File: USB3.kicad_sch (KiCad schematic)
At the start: 20 parts, among them J1 10152803-00011LF, U1 NCP360SNT1G, U2 TUSB321RWBR, U7 TUSB542RWQR

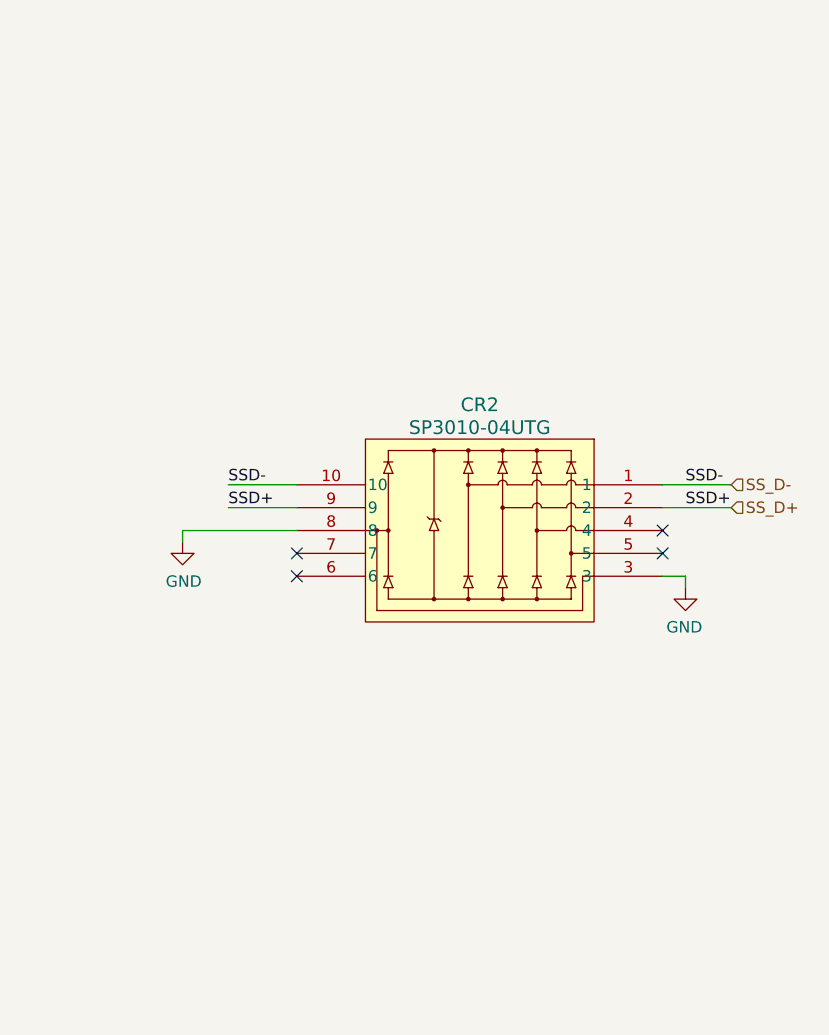
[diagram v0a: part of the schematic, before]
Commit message: start reworking the usb3c to add ESD and better impedance matching
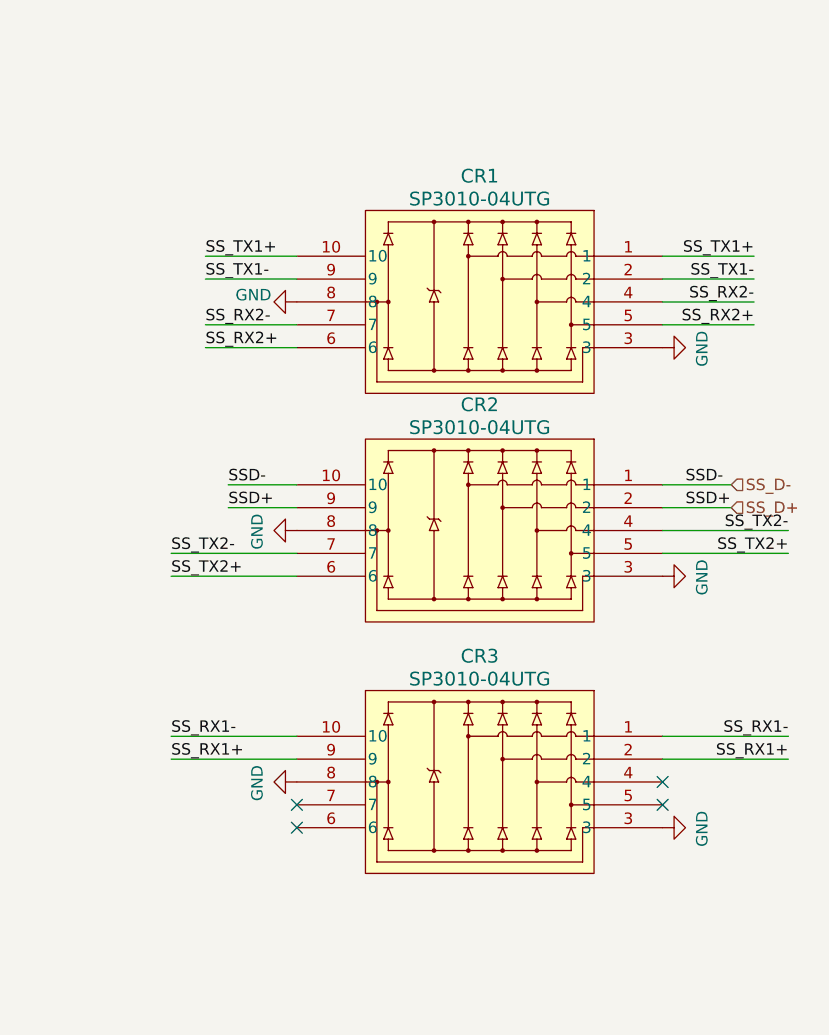
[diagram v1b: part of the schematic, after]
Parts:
- added CR1, CR3: SP3010-04UTG, SP3010:UDFEN-10_MO229_LTF, symbol SP3010-04UTG:SP3010-04UTG
- C69, C70, C71, C72, C73, C74, C8, C9: footprint Capacitor_SMD:C_0402_1005Metric -> Capacitor_SMD:C_0201_0603Metric
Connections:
- net GND: now also CR1.3, CR1.8, CR3.3, CR3.8
- net SS_RX1+: now also CR3.2, CR3.9
- net SS_RX1-: now also CR3.1, CR3.10
- net SS_RX2+: now also CR1.5, CR1.6
- net SS_RX2-: now also CR1.4, CR1.7
- net SS_TX1+: now also CR1.1, CR1.10
- net SS_TX1-: now also CR1.2, CR1.9
- net SS_TX2+: now also CR2.5, CR2.6
- net SS_TX2-: now also CR2.4, CR2.7

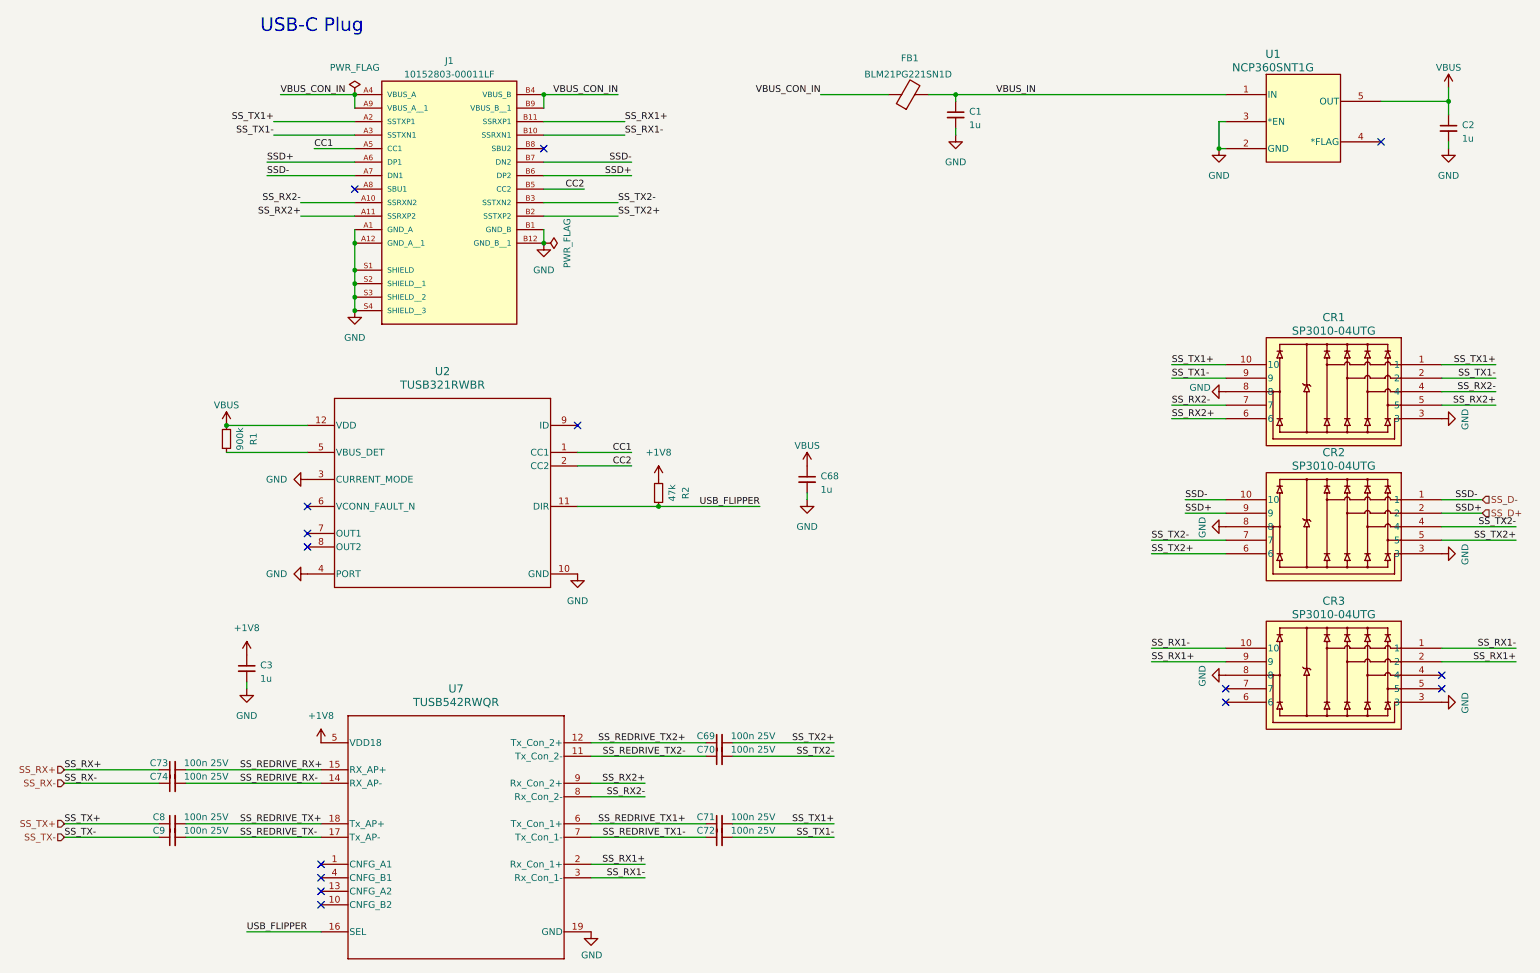
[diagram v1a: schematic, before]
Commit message: start implementing SML feedback
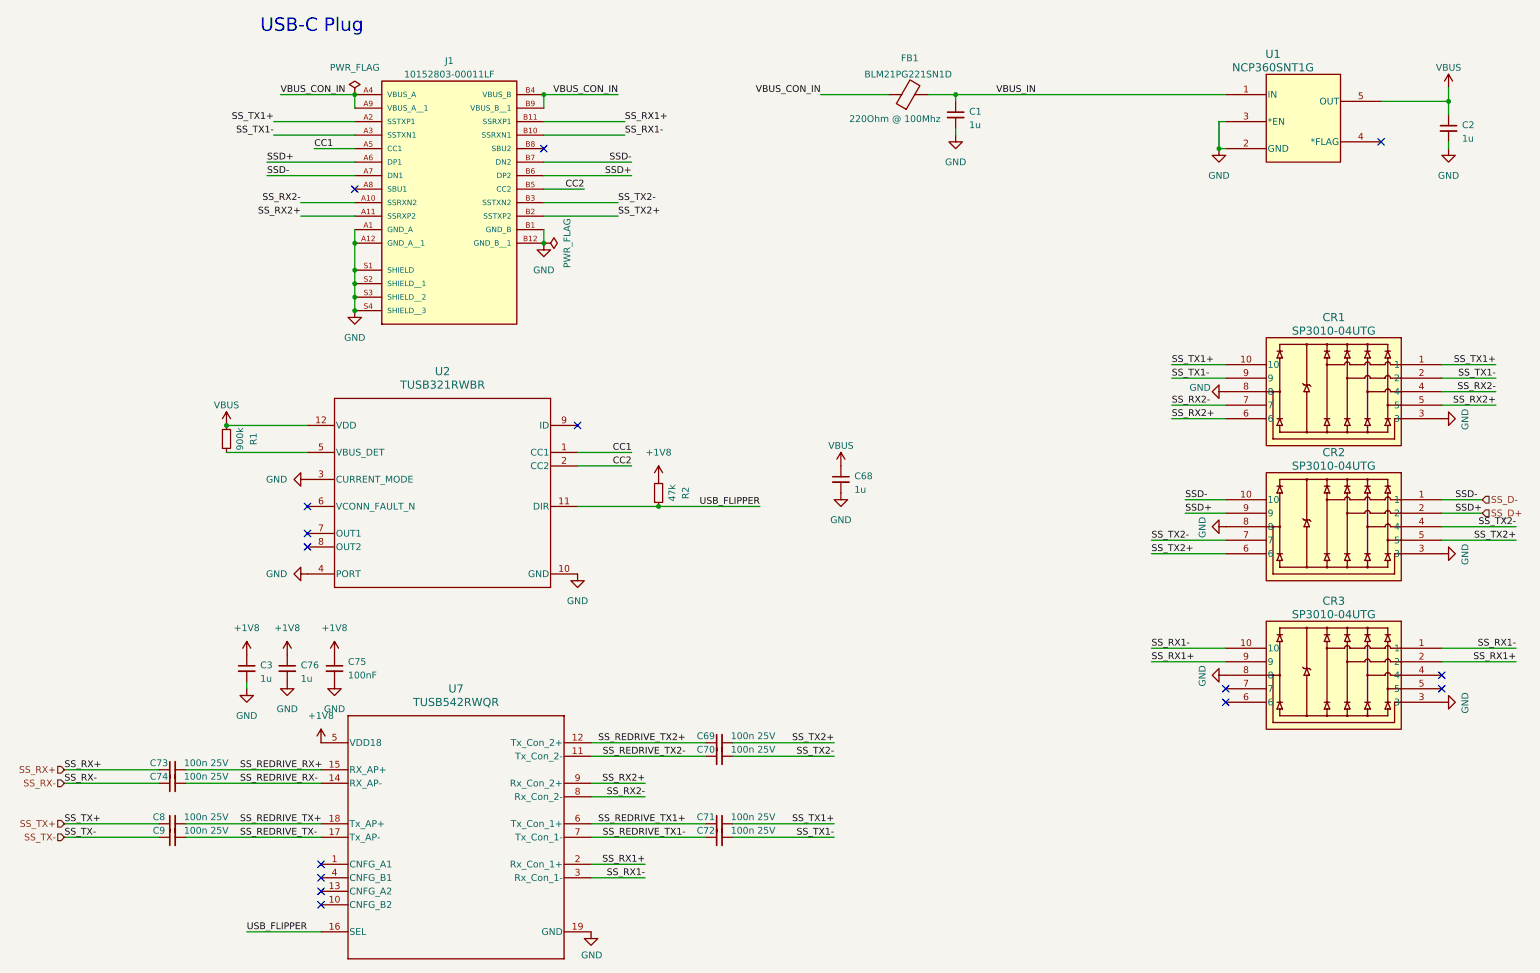
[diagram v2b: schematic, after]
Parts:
- added C75: 100nF, Capacitor_SMD:C_0402_1005Metric, symbol Device:C_Small
- added C76: 1u, Capacitor_SMD:C_0402_1005Metric, symbol Device:C_Small
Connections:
- net +1V8: now also C75.1, C76.1
- net GND: now also C75.2, C76.2
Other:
- moved on the sheet: C68

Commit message: implement all SML review nits
hopefully
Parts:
- C69, C70, C71, C72, C73, C74, C8, C9: footprint Capacitor_SMD:C_0201_0603Metric -> logic_analyzer:C_0201_0603Metric_USB
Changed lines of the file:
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@@
 			)
 		)
-		(property "Footprint" "Capacitor_SMD:C_0201_0603Metric"
+		(property "Footprint" "logic_analyzer:C_0201_0603Metric_USB"
 			(at 118.11 173.99 0)
 			(effects
@@
 			)
 		)
-		(property "Footprint" "Capacitor_SMD:C_0201_0603Metric"
+		(property "Footprint" "logic_analyzer:C_0201_0603Metric_USB"
 			(at 118.11 158.75 0)
 			(effects
@@
 			)
 		)
-		(property "Footprint" "Capacitor_SMD:C_0201_0603Metric"
+		(property "Footprint" "logic_analyzer:C_0201_0603Metric_USB"
 			(at 15.24 161.29 0)
 			(effects
@@
 			)
 		)
-		(property "Footprint" "Capacitor_SMD:C_0201_0603Metric"
+		(property "Footprint" "logic_analyzer:C_0201_0603Metric_USB"
 			(at 15.24 171.45 0)
 			(effects
@@
 			)
 		)
-		(property "Footprint" "Capacitor_SMD:C_0201_0603Metric"
+		(property "Footprint" "logic_analyzer:C_0201_0603Metric_USB"
 			(at 15.24 173.99 0)
 			(effects
@@
 			)
 		)
-		(property "Footprint" "Capacitor_SMD:C_0201_0603Metric"
+		(property "Footprint" "logic_analyzer:C_0201_0603Metric_USB"
 			(at 118.11 171.45 0)
 			(effects
@@
 			)
 		)
-		(property "Footprint" "Capacitor_SMD:C_0201_0603Metric"
+		(property "Footprint" "logic_analyzer:C_0201_0603Metric_USB"
 			(at 15.24 163.83 0)
 			(effects
@@
 			)
 		)
-		(property "Footprint" "Capacitor_SMD:C_0201_0603Metric"
+		(property "Footprint" "logic_analyzer:C_0201_0603Metric_USB"
 			(at 118.11 156.21 0)
 			(effects
